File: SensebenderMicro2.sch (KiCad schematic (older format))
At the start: 38 parts, among them P1 Debug, P2 MYSX_1.2, P3 Antenna, Q1 SI2333DDS-T1-GE3, U1 ATSAMD21E, U2 MCP1703T-3302E, U3 NRF24L01, U4 RFM69HW, U5 ATSHA204A, U6 AT45DB041E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

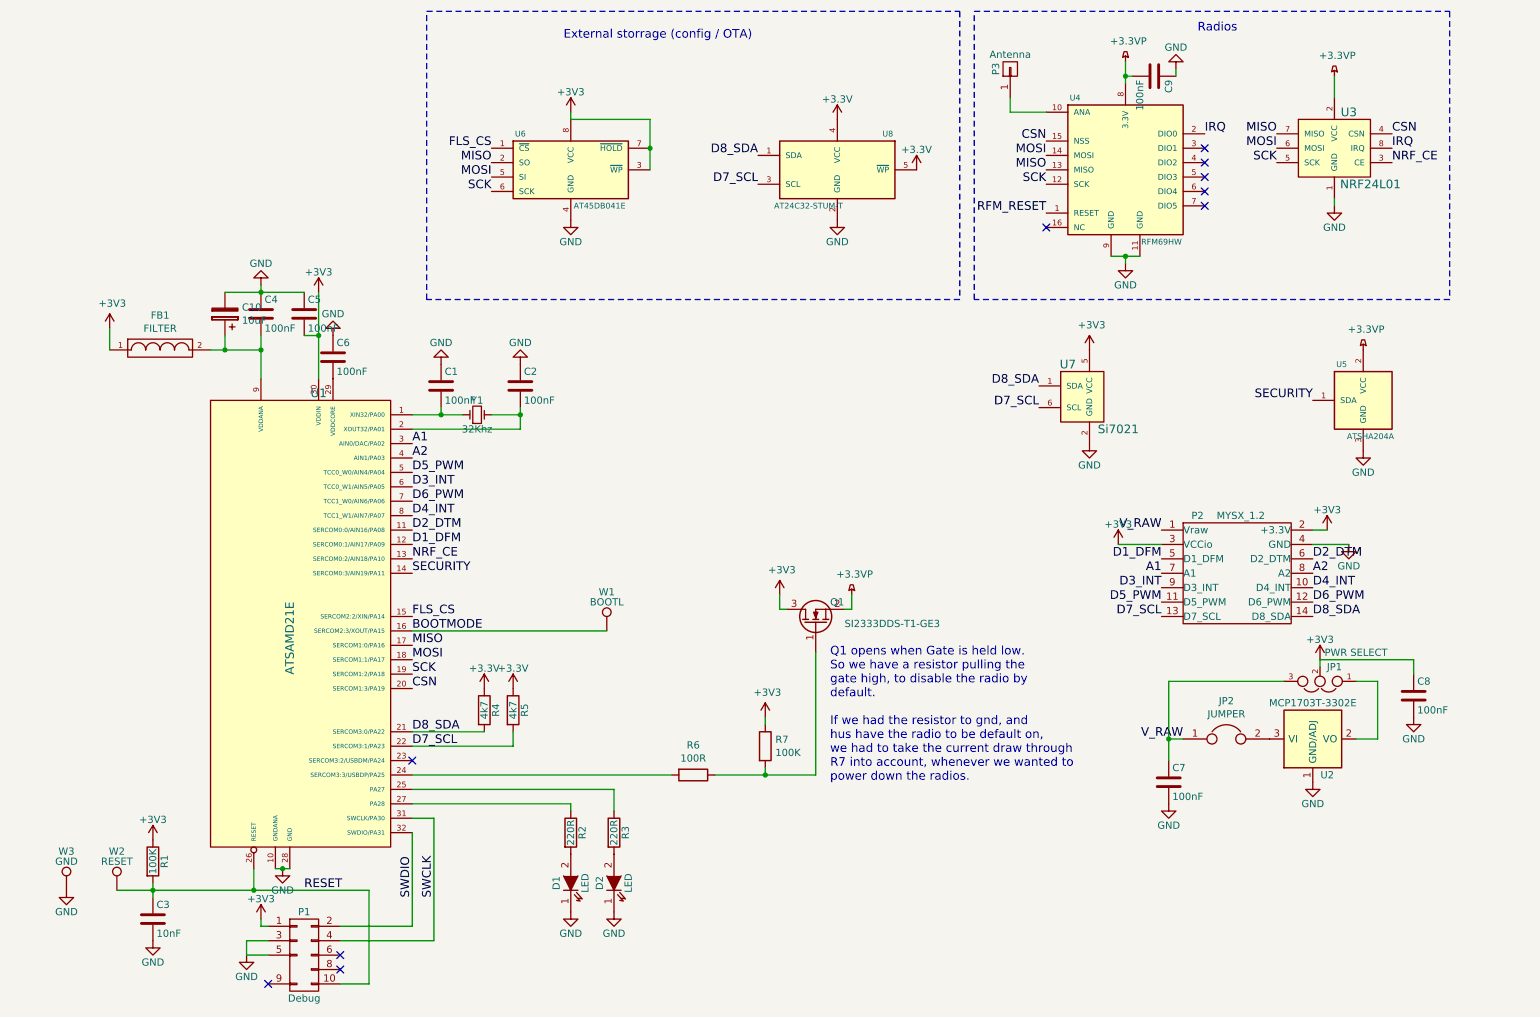
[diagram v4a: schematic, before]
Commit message: added reset / DIO5 connections to RFM69
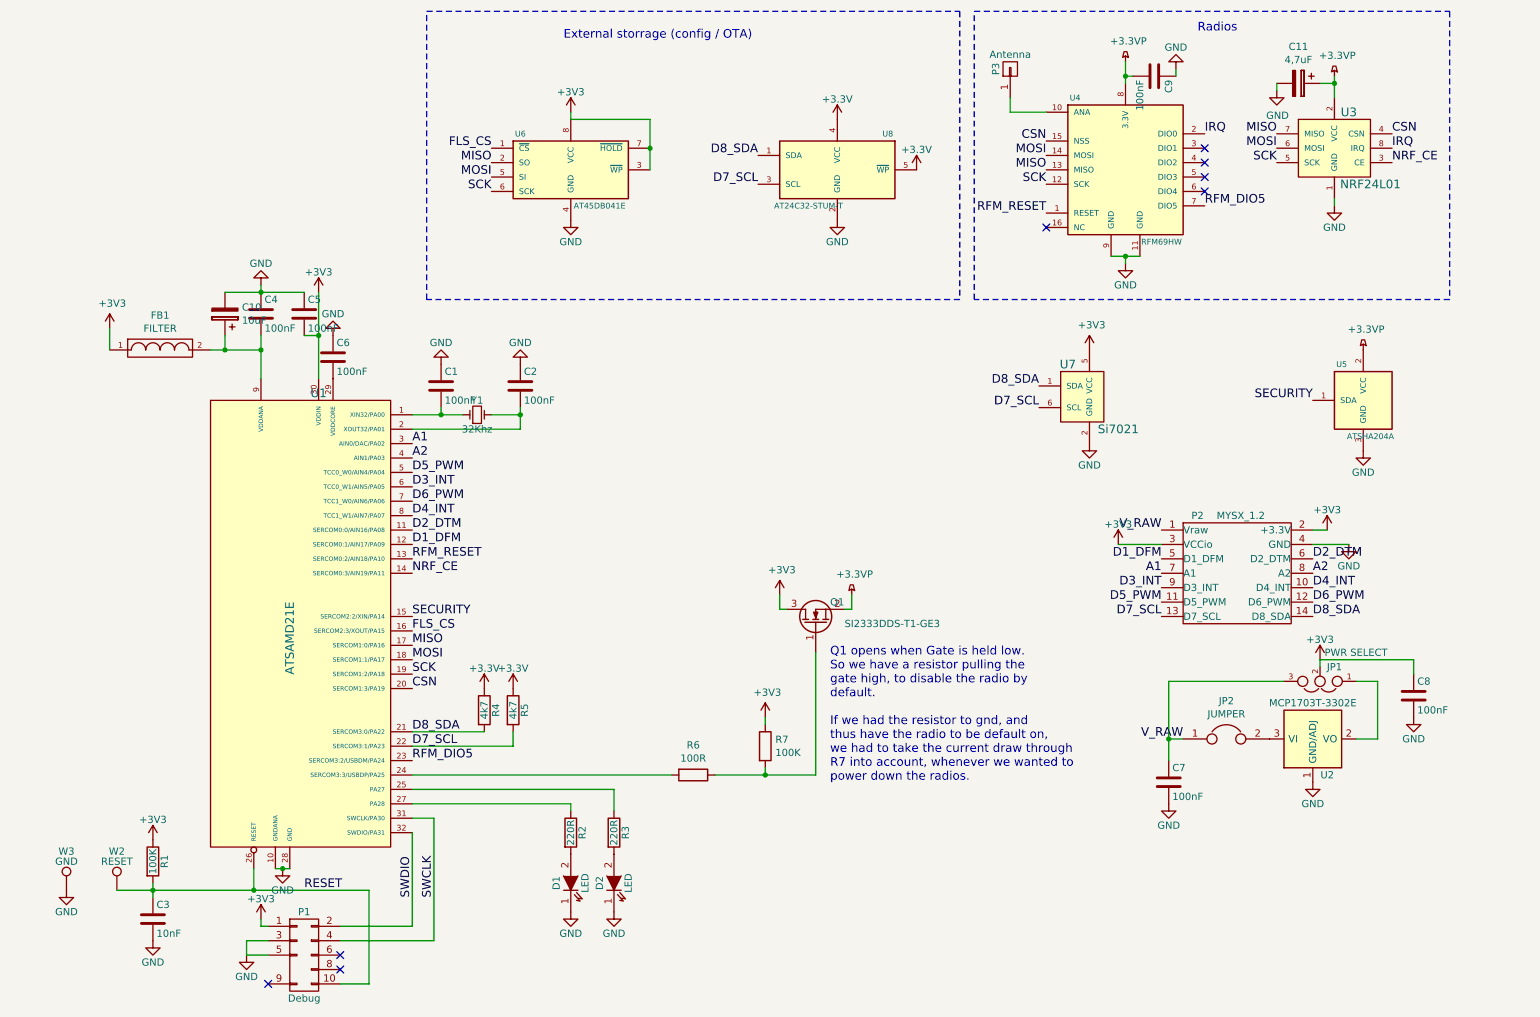
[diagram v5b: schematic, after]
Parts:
- removed W1: BOOTL, Measurement_Points:Measurement_Point_Round-SMD-Pad_Small, symbol TEST_1P
- added C11: 4,7uF, Capacitors_SMD:C_0603, symbol CP
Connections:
- net BOOTMODE is gone; now on net FLS_CS: U1.16 (SERCOM2:3/XOUT/PA15)
- net +3.3VP: now also C11.1
- net FLS_CS: no longer U1.15 (SERCOM2:2/XIN/PA14)
- net GND: now also C11.2
- net NRF_CE: now also U1.14 (SERCOM0:3/AIN19/PA11); no longer U1.13 (SERCOM0:2/AIN18/PA10)
- net RFM_RESET: now also U1.13 (SERCOM0:2/AIN18/PA10)
- net SECURITY: now also U1.15 (SERCOM2:2/XIN/PA14); no longer U1.14 (SERCOM0:3/AIN19/PA11)
- net RFM_DIO5: now reaches U4.7 (DIO5)
- net RFM_DIO5: now also U1.23 (SERCOM3:2/USBDM/PA24)
- no-connect marks 10 -> 8
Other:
- note added: "Q1 opens when Gate is held low. \nSo we have a resistor pulling the \ngate high, to disable the radio by\ndefault.\n\nIf we had the resistor to gnd, and \nthus have the radio to be default on,\nwe had to take the current draw through\nR7 into account, whenever we wanted to\npower down the radios."
- note removed: "Q1 opens when Gate is held low. \nSo we have a resistor pulling the \ngate high, to disable the radio by\ndefault.\n\nIf we had the resistor to gnd, and \nhus have the radio to be default on,\nwe had to take the current draw through\nR7 into account, whenever we wanted to\npower down the radios."
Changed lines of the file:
@@
 V_RAW
-$Comp
-L ATSAMD21E U1
-U 1 1 56B7791C
-P 2750 4700
-F 0 "U1" H 2950 6200 60  0000 C CNN
-F 1 "ATSAMD21E" V 2750 4500 60  0000 C CNN
-F 2 "Housings_QFP:TQFP-32_7x7mm_Pitch0.8mm" H 1950 3250 60  0001 C CNN
-F 3 "" H 1950 3250 60  0000 C CNN
-	1    2750 4700
-	1    0    0    -1
-$EndComp
 $Comp
 L C C1
@@
 	1    0    0    -1
 $EndComp
-Text Label 3600 4450 0    60   ~ 0
-SECURITY
 Text Label 9850 3250 2    60   ~ 0
 SECURITY
@@
 	1    0    0    -1
 $EndComp
-Text Label 3600 4750 0    60   ~ 0
+Text Label 3600 4850 0    60   ~ 0
 FLS_CS
 $Comp
@@
 	-1   0    0    1
 $EndComp
-Text Label 3600 4850 0    60   ~ 0
-BOOTMODE
 $Comp
 L GND #PWR028
@@
 	1    0    0    -1
 $EndComp
-Text Label 3600 4350 0    60   ~ 0
+Text Label 3600 4450 0    60   ~ 0
 NRF_CE
 NoConn ~ 9100 1500
@@
 NoConn ~ 9100 1700
 NoConn ~ 9100 1800
-NoConn ~ 9100 1900
 NoConn ~ 8000 2050
 $Comp
@@
 	1    8900 950
 	-1   0    0    1
-$EndComp
-$Comp
-L TEST_1P W1
-U 1 1 56BC6E9C
-P 4950 4850
-F 0 "W1" H 4950 5120 50  0000 C CNN
-F 1 "BOOTL" H 4950 5050 50  0000 C CNN
-F 2 "Measurement_Points:Measurement_Point_Round-SMD-Pad_Small" H 5150 4850 50  0001 C CNN
-F 3 "" H 5150 4850 50  0000 C CNN
-	1    4950 4850
-	1    0    0    -1
 $EndComp
 Text Notes 9050 700  0    60   ~ 0
@@
 07 00 85 88 3B 00 28 44 DC 01 40 21 E2 0E 00 0A 11 77 00 50 88 B8 03 80 42 C4 1D 00 14 22 EE 00
 A0 10 71 07 00 85 88 3B 00 28 F4 2F 6E 0E 73 66 69 F5 31 42 00 00 00 00 49 45 4E 44 AE 42 60 82
-B0
+78
 EndData
 $EndBitmap
@@
 	1    0    0    -1
 $EndComp
-NoConn ~ 3600 5750
 $Comp
 L R R6
@@
 Wire Wire Line
 	2300 2500 2850 2500
-Wire Wire Line
-	3600 4850 4950 4850
 Wire Wire Line
 	4700 6100 4700 6050
@@
 Connection ~ 6050 5850
 Text Notes 6500 5900 0    60   ~ 0
-Q1 opens when Gate is held low. \nSo we have a resistor pulling the \ngate high, to disable the radio by\ndefault.\n\nIf we had the resistor to gnd, and \nhus have the radio to be default on,\nwe had to take the current draw through\nR7 into account, whenever we wanted to\npower down the radios.
+Q1 opens when Gate is held low. \nSo we have a resistor pulling the \ngate high, to disable the radio by\ndefault.\n\nIf we had the resistor to gnd, and \nthus have the radio to be default on,\nwe had to take the current draw through\nR7 into account, whenever we wanted to\npower down the radios.
 Wire Wire Line
 	10300 5200 10300 5600
@@
 Wire Wire Line
 	10550 5050 10550 5150
+$Comp
+L CP C11
+U 1 1 5761A4FA
+P 9750 1050
+F 0 "C11" V 9495 1050 50  0000 C CNN
+F 1 "4,7uF" V 9586 1050 50  0000 C CNN
+F 2 "Capacitors_SMD:C_0603" H 9788 900 50  0001 C CNN
+F 3 "" H 9750 1050 50  0000 C CNN
+	1    9750 1050
+	0    1    1    0
+$EndComp
+Wire Wire Line
+	9900 1050 10000 1050
+Connection ~ 10000 1050
+$Comp
+L GND #PWR041
+U 1 1 5761A76F
+P 9600 1100
+F 0 "#PWR041" H 9600 850 50  0001 C CNN
+F 1 "GND" H 9605 927 50  0000 C CNN
+F 2 "" H 9600 1100 50  0000 C CNN
+F 3 "" H 9600 1100 50  0000 C CNN
+	1    9600 1100
+	1    0    0    -1
+$EndComp
+Wire Wire Line
+	9600 1100 9600 1050
+Text Label 3600 4750 0    60   ~ 0
+SECURITY
+$Comp
+L ATSAMD21E U1
+U 1 1 56B7791C
+P 2750 4700
+F 0 "U1" H 2950 6200 60  0000 C CNN
+F 1 "ATSAMD21E" V 2750 4500 60  0000 C CNN
+F 2 "Housings_QFP:TQFP-32_7x7mm_Pitch0.8mm" H 1950 3250 60  0001 C CNN
+F 3 "" H 1950 3250 60  0000 C CNN
+	1    2750 4700
+	1    0    0    -1
+$EndComp
+Text Label 9100 1900 0    60   ~ 0
+RFM_DIO5
+Text Label 3600 4350 0    60   ~ 0
+RFM_RESET
+Text Label 3600 5750 0    60   ~ 0
+RFM_DIO5
 $EndSCHEMATC

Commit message: Updated to use MYSX2.x with reset
Also shuffled peripherals around on the samd, to make routing easier
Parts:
- removed P1: Debug, mysensors_connectors:Cortex_M_Debug_Connector, symbol Debug
- added C12: C, Capacitors_SMD:C_0603, symbol C
- added W3: SWCLK, Measurement_Points:Measurement_Point_Round-SMD-Pad_Small, symbol TEST_1P
- added W4: SWDIO, Measurement_Points:Measurement_Point_Round-SMD-Pad_Small, symbol TEST_1P
- added W5: VCC, Measurement_Points:Measurement_Point_Round-SMD-Pad_Small, symbol TEST_1P
- P2: value MYSX_1.2 -> MYSX_2.4; symbol MYSX_1.3 -> MYSX_2.4
- renumbered W3 to W1
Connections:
- net +3V3: now also W5.1
- net A1: now also P2.15 (D9_A3); no longer P2.7 (A1)
- net A2: now also P2.16 (D10_A4); no longer P2.8 (A2)
- net D1_DFM: now also U1.6 (TCC0_W1/AIN5/PA05); no longer U1.12 (SERCOM0:1/AIN17/PA09)
- net D2_DTM: now also U1.5 (TCC0_W0/AIN4/PA04); no longer U1.11 (SERCOM0:0/AIN16/PA08)
- net D3_INT: now also U1.7 (TCC1_W0/AIN6/PA06); no longer U1.6 (TCC0_W1/AIN5/PA05)
- net D5_PWM: now also U1.11 (SERCOM0:0/AIN16/PA08); no longer U1.5 (TCC0_W0/AIN4/PA04)
- net D6_PWM: now also U1.13 (SERCOM0:2/AIN18/PA10); no longer U1.7 (TCC1_W0/AIN6/PA06)
- net D7_SCL: now also U1.18 (SERCOM1:1/PA17); no longer U1.22 (SERCOM3:1/PA23)
- net D8_SDA: now also U1.17 (SERCOM1:0/PA16); no longer U1.21 (SERCOM3:0/PA22)
- net IRQ: now also U1.12 (SERCOM0:1/AIN17/PA09)
- net MISO: now also U1.23 (SERCOM3:2/USBDM/PA24); no longer U1.17 (SERCOM1:0/PA16)
- net MOSI: now also U1.21 (SERCOM3:0/PA22); no longer U1.18 (SERCOM1:1/PA17)
- net RESET: now also C12.1
- net SCK: now also U1.22 (SERCOM3:1/PA23); no longer U1.19 (SERCOM1:2/PA18)
- net SWCLK: now also W3.1
- net SWDIO: now also W4.1
- net at U1.24 (SERCOM3:3/USBDP/PA25): now also R3.1; no longer R6.2
- net at U1.25 (PA27): now also R2.1; no longer R3.1
- net at U1.27 (PA28): now also R6.2; no longer R2.1
- net +3.3VA: now reaches C10.1, C4.2, FB1.2, U1.9 (VDDANA)
- net NRF_CE renamed LEGACY_ID
- net LEGACY_ID: now also P2.8 (LEGACY_ID); no longer U3.3 (CE)
- net RFM_DIO5 renamed NRF_CE_RFM_DIO5
- net NRF_CE_RFM_DIO5: now also U1.19 (SERCOM1:2/PA18), U3.3 (CE); no longer U1.23 (SERCOM3:2/USBDM/PA24)
- net RFM_RESET: no longer names the net of U4.1 (RESET)
- net RFM_RESET: no longer U1.13 (SERCOM0:2/AIN18/PA10)
- new net RST: C12.2, P2.7 (RST)
- no-connect marks 8 -> 6
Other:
- moved on the sheet: R4, R5

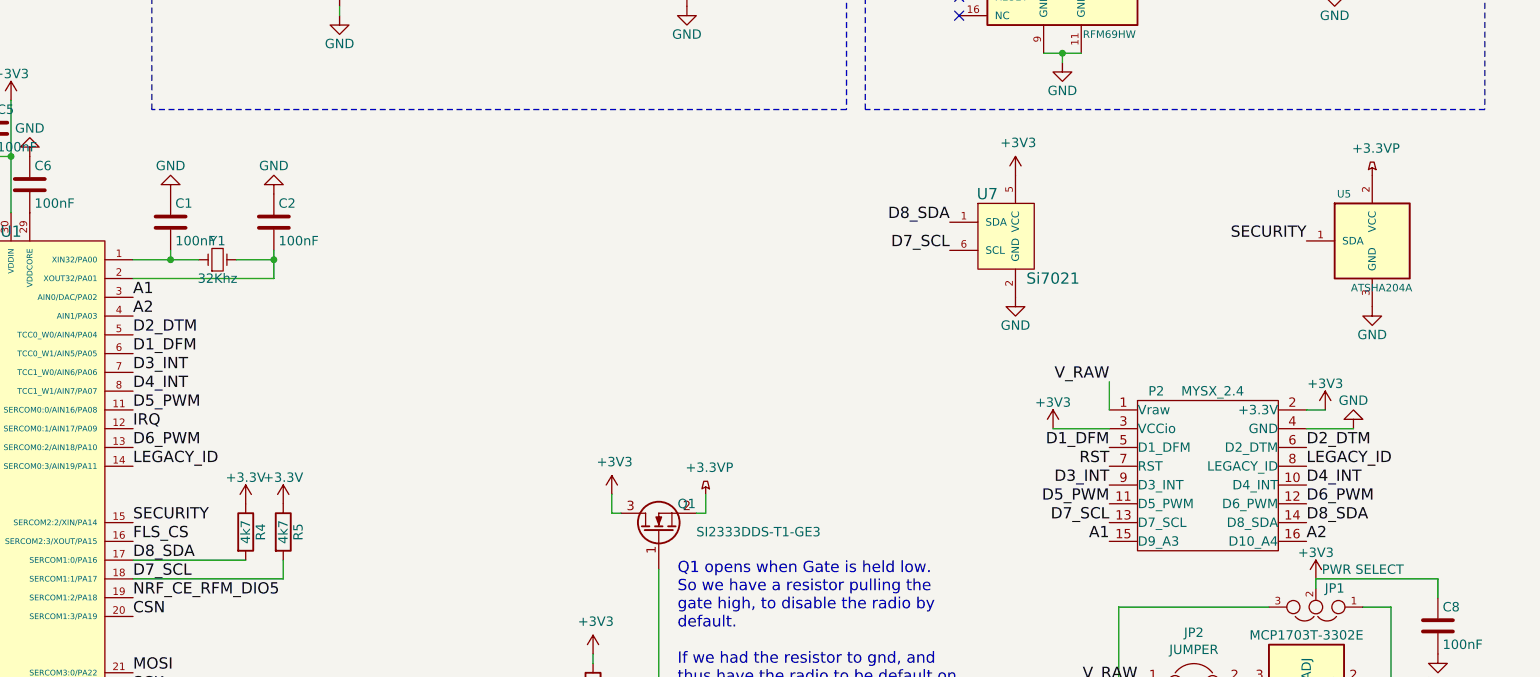
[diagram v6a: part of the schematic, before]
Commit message: recreated routing with better ground plane
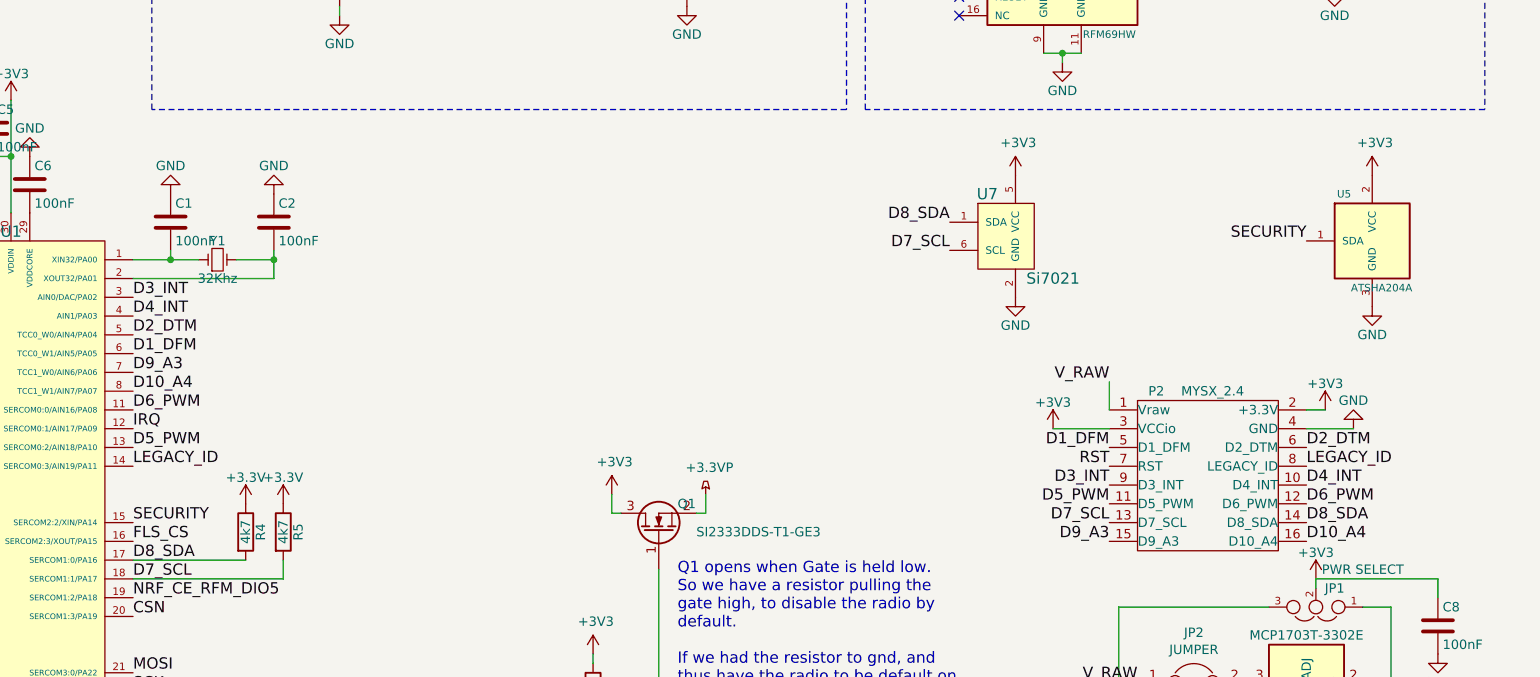
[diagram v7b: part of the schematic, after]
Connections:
- net +3.3VP: no longer U5.2 (VCC)
- net +3V3: now also U5.2 (VCC)
- net D3_INT: now also U1.3 (AIN0/DAC/PA02); no longer U1.7 (TCC1_W0/AIN6/PA06)
- net D4_INT: now also U1.4 (AIN1/PA03); no longer U1.8 (TCC1_W1/AIN7/PA07)
- net D5_PWM: now also U1.13 (SERCOM0:2/AIN18/PA10); no longer U1.11 (SERCOM0:0/AIN16/PA08)
- net D6_PWM: now also U1.11 (SERCOM0:0/AIN16/PA08); no longer U1.13 (SERCOM0:2/AIN18/PA10)
- net A1 renamed D9_A3
- net D9_A3: now also U1.7 (TCC1_W0/AIN6/PA06); no longer U1.3 (AIN0/DAC/PA02)
- net A2 renamed D10_A4
- net D10_A4: now also U1.8 (TCC1_W1/AIN7/PA07); no longer U1.4 (AIN1/PA03)
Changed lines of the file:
@@
 Text Label 9850 4350 0    60   ~ 0
 D2_DTM
+Text Label 3600 4050 0    60   ~ 0
+D10_A4
+Text Label 3600 3550 0    60   ~ 0
+D3_INT
+Text Label 3600 4150 0    60   ~ 0
+D6_PWM
 Text Label 3600 3650 0    60   ~ 0
-A2
-Text Label 3600 4150 0    60   ~ 0
-D5_PWM
+D4_INT
 Text Label 3600 3950 0    60   ~ 0
-D3_INT
-Text Label 3600 4350 0    60   ~ 0
-D6_PWM
-Text Label 3600 4050 0    60   ~ 0
-D4_INT
-Text Label 3600 3550 0    60   ~ 0
-A1
+D9_A3
 Text Label 8800 4650 2    60   ~ 0
 D5_PWM
@@
 D3_INT
 Text Label 8800 4850 2    60   ~ 0
-A1
+D9_A3
 Text Label 9850 4850 0    60   ~ 0
-A2
+D10_A4
 Text Label 9850 4550 0    60   ~ 0
 D4_INT
@@
 $EndComp
 $Comp
-L +3.3VP #PWR037
-U 1 1 57264480
-P 10200 2900
-F 0 "#PWR037" H 10350 2850 50  0001 C CNN
-F 1 "+3.3VP" H 10220 3043 50  0000 C CNN
-F 2 "" H 10200 2900 50  0000 C CNN
-F 3 "" H 10200 2900 50  0000 C CNN
-	1    10200 2900
-	1    0    0    -1
-$EndComp
-$Comp
 L R R6
 U 1 1 57279B05
@@
 	6400 5850 5700 5850
 $Comp
-L +3V3 #PWR038
+L +3V3 #PWR037
 U 1 1 5727A1DE
 P 6050 5450
-F 0 "#PWR038" H 6050 5300 50  0001 C CNN
+F 0 "#PWR037" H 6050 5300 50  0001 C CNN
 F 1 "+3V3" H 6065 5623 50  0000 C CNN
 F 2 "" H 6050 5450 50  0000 C CNN
@@
 Connection ~ 10000 1050
 $Comp
-L GND #PWR039
+L GND #PWR038
 U 1 1 5761A76F
 P 9600 1100
-F 0 "#PWR039" H 9600 850 50  0001 C CNN
+F 0 "#PWR038" H 9600 850 50  0001 C CNN
 F 1 "GND" H 9605 927 50  0000 C CNN
 F 2 "" H 9600 1100 50  0000 C CNN
@@
 LEGACY_ID
 $Comp
-L +3.3VA #PWR040
+L +3.3VA #PWR039
 U 1 1 5828CA22
 P 2300 2900
-F 0 "#PWR040" H 2300 2750 50  0001 C CNN
+F 0 "#PWR039" H 2300 2750 50  0001 C CNN
 F 1 "+3.3VA" H 2315 3073 50  0000 C CNN
 F 2 "" H 2300 2900 50  0000 C CNN
@@
 $EndComp
 $Comp
-L +3V3 #PWR041
+L +3V3 #PWR040
 U 1 1 582A3CE8
 P 950 6650
-F 0 "#PWR041" H 950 6500 50  0001 C CNN
+F 0 "#PWR040" H 950 6500 50  0001 C CNN
 F 1 "+3V3" H 965 6823 50  0000 C CNN
 F 2 "" H 950 6650 50  0000 C CNN
@@
 	-1   0    0    1
 $EndComp
+$Comp
+L +3V3 #PWR041
+U 1 1 582F12E3
+P 10200 2900
+F 0 "#PWR041" H 10200 2750 50  0001 C CNN
+F 1 "+3V3" H 10215 3073 50  0000 C CNN
+F 2 "" H 10200 2900 50  0000 C CNN
+F 3 "" H 10200 2900 50  0000 C CNN
+	1    10200 2900
+	1    0    0    -1
+$EndComp
+Text Label 3600 4350 0    60   ~ 0
+D5_PWM
 $EndSCHEMATC
